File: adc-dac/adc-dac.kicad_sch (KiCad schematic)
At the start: 49 parts, among them J1 Conn_02x03_Odd_Even, J2 Conn_02x01, J3 Conn_01x06, J4 Conn_01x06, J5 Conn_01x06, J6 Conn_01x06, J7 Conn_01x06, J8 Conn_01x06, SW1 SW_SPDT, U1 AD5593R, U2 ADS122C04IPW, U3 TS5A23159DGS, U4 TS5A23159DGS, U5 TLV75801PDBV, U6 LM321

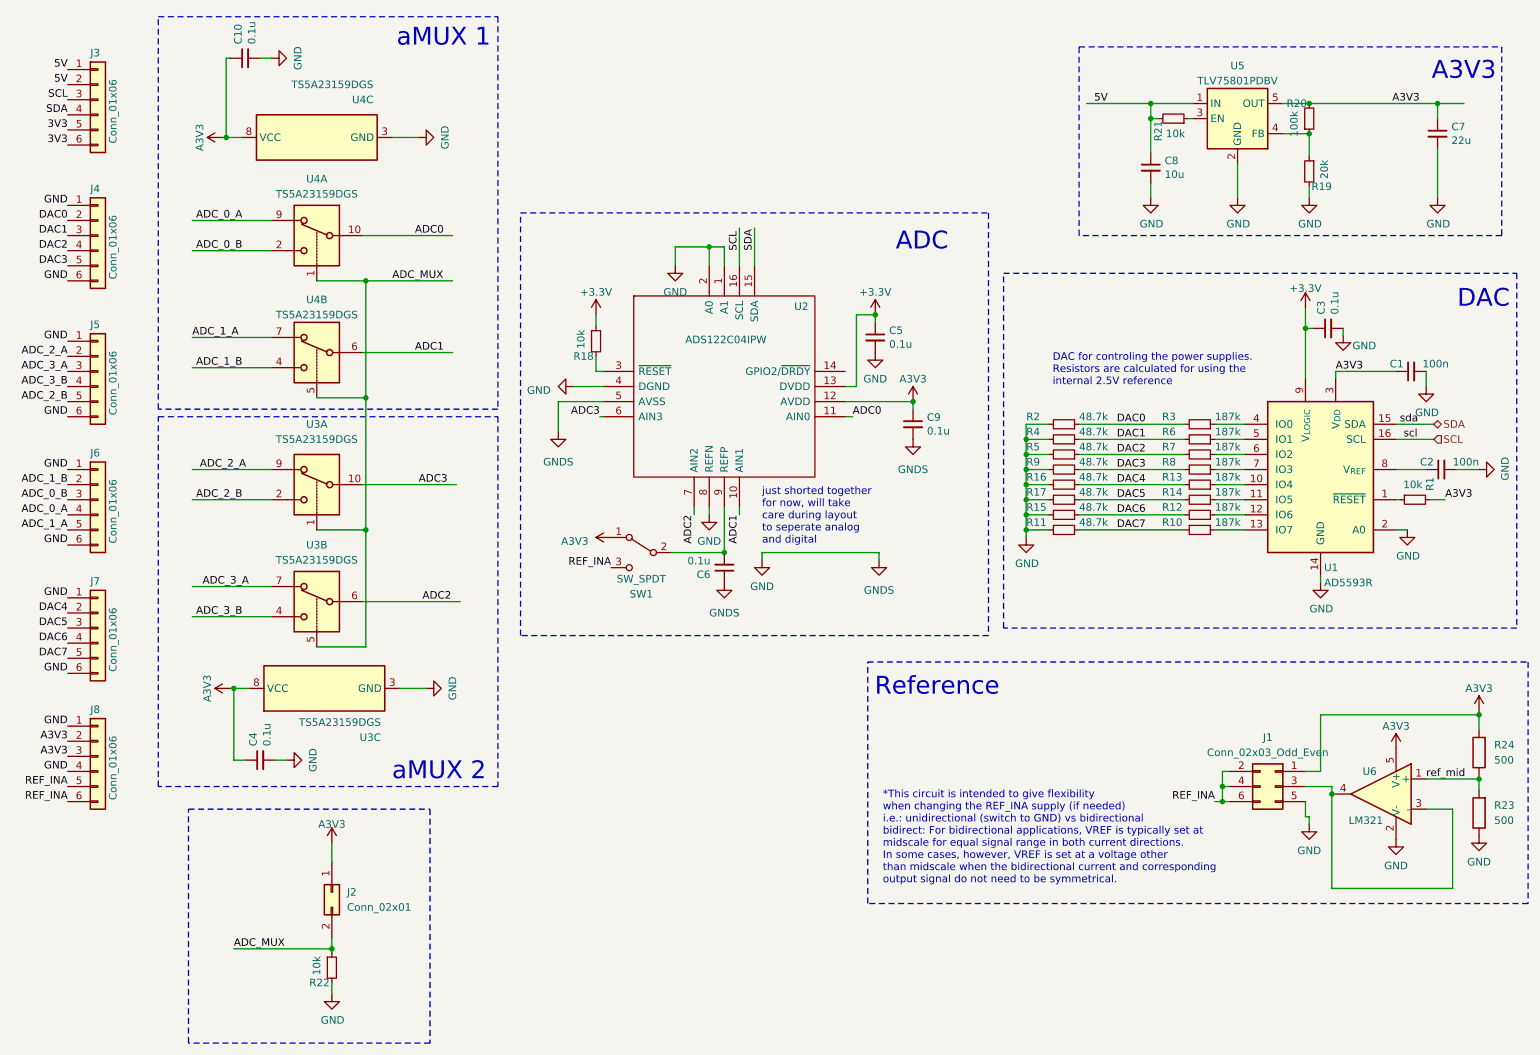
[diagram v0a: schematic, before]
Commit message: re-arranged adc/dac and routed to the cgs
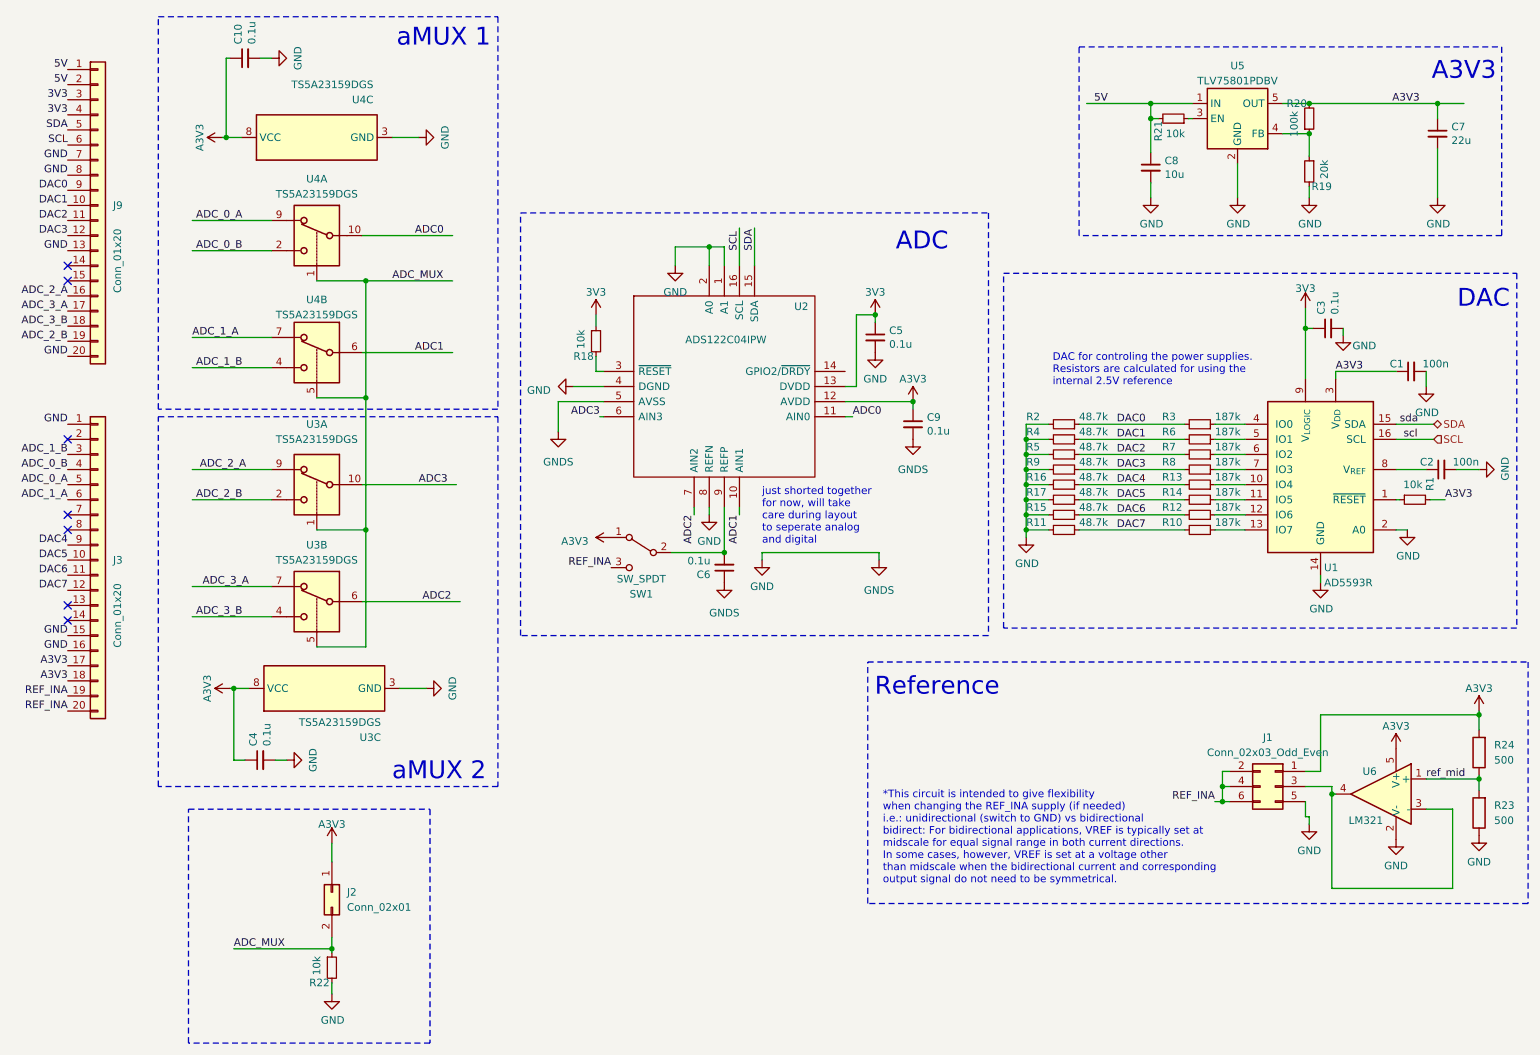
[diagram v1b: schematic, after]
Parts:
- removed J3, J4, J5, J6, J7, J8: Conn_01x06, Connector_PinHeader_1.27mm:PinHeader_1x06_P1.27mm_Vertical, symbol Connector_Generic:Conn_01x06
- added J3, J9: Conn_01x20, Connector_PinHeader_1.27mm:PinHeader_1x20_P1.27mm_Vertical, symbol Connector_Generic:Conn_01x20
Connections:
- net +3.3V is gone; now on net 3V3: C3.1, C5.1, R18.1, U1.9 (V_{LOGIC}), U2.13 (DVDD)
- net 3V3: now also J9.3 (Pin_3), J9.4 (Pin_4)
- net 5V: now also J9.1 (Pin_1), J9.2 (Pin_2)
- net A3V3: now also J3.17 (Pin_17), J3.18 (Pin_18)
- net ADC_0_A: now also J3.5 (Pin_5)
- net ADC_0_B: now also J3.4 (Pin_4)
- net ADC_1_A: now also J3.6 (Pin_6)
- net ADC_1_B: now also J3.3 (Pin_3)
- net ADC_2_A: now also J9.16 (Pin_16)
- net ADC_2_B: now also J9.19 (Pin_19)
- net ADC_3_A: now also J9.17 (Pin_17)
- net ADC_3_B: now also J9.18 (Pin_18)
- net DAC0: now also J9.9 (Pin_9)
- net DAC1: now also J9.10 (Pin_10)
- net DAC2: now also J9.11 (Pin_11)
- net DAC3: now also J9.12 (Pin_12)
- net DAC4: now also J3.9 (Pin_9)
- net DAC5: now also J3.10 (Pin_10)
- net DAC6: now also J3.11 (Pin_11)
- net DAC7: now also J3.12 (Pin_12)
- net GND: now also J3.1 (Pin_1), J3.15 (Pin_15), J3.16 (Pin_16), J9.13 (Pin_13), J9.20 (Pin_20), J9.7 (Pin_7), J9.8 (Pin_8)
- net REF_INA: now also J3.19 (Pin_19), J3.20 (Pin_20)
- net SCL: now also J9.6 (Pin_6)
- net SDA: now also J9.5 (Pin_5)
- no-connect marks 0 -> 7
